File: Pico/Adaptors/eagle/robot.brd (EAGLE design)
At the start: 63.9 x 22.1 mm, 23 parts, among them J1 JST-2P-SMD-PW-3410050P1, U1 HC_05

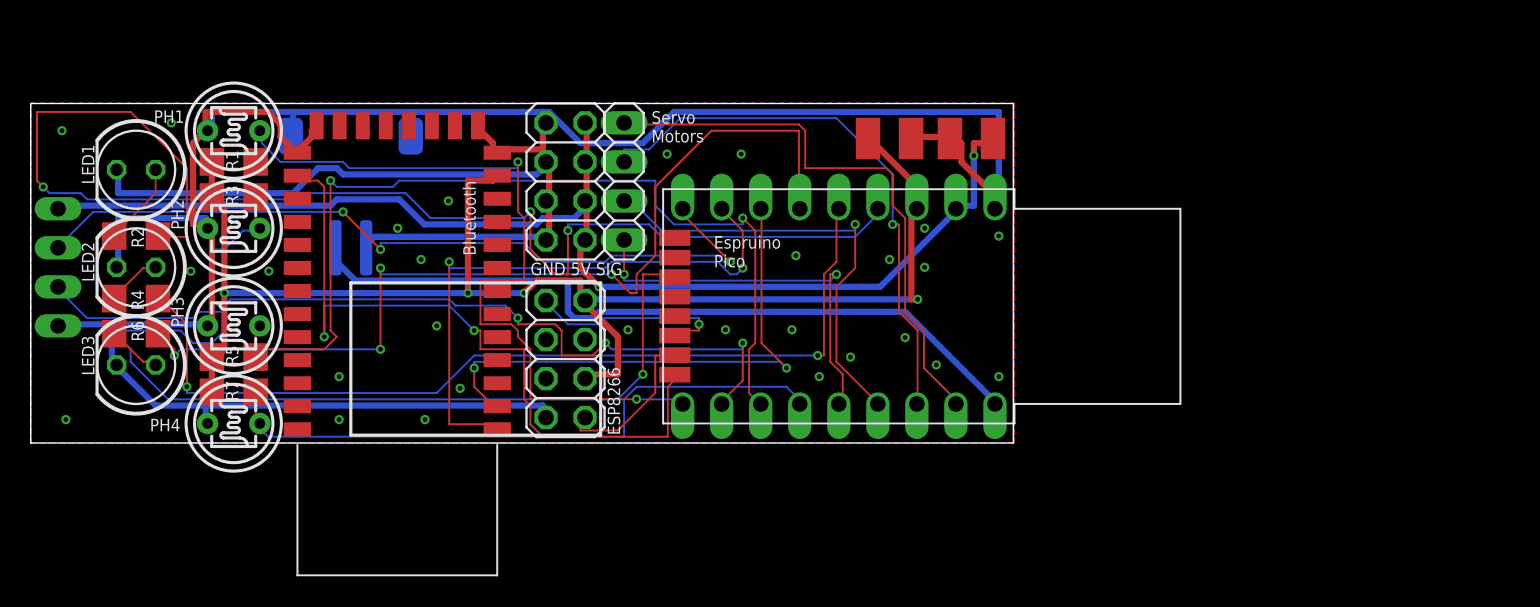
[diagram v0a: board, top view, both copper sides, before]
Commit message: added another ultrasonic sensor, pins down the side, and ADNS5050 optical sensor
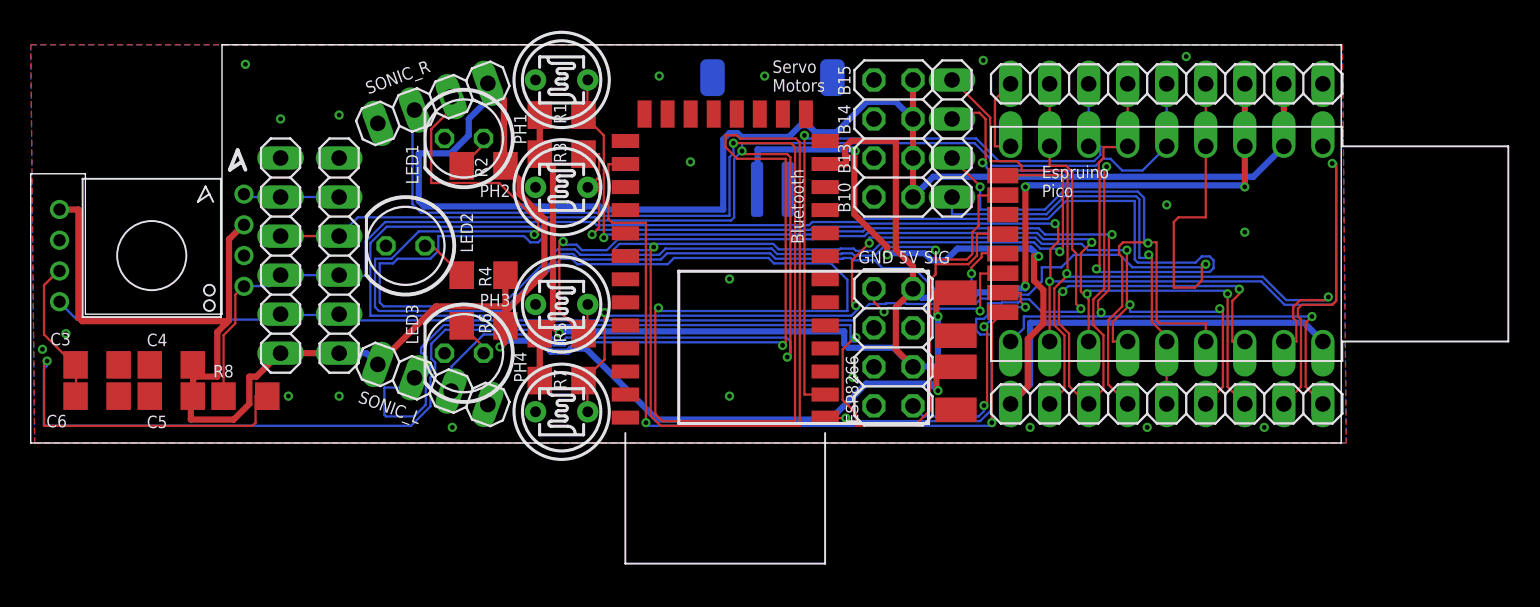
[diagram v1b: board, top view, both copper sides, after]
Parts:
- removed HC-SR04: (no value), pinhead:1X04
- added C3: 3.3uF, rcl:C1206
- added C4: 4.7uF, rcl:C1206
- added C5, C6: 0.1uF, rcl:C1206
- added JP3, JP4: (no value), pinhead:1X06
- added JP5, JP6: (no value), pinhead:1X09
- added R8: 3k, rcl:R1206
- added SONIC_L, SONIC_R: (no value), pinhead:1X04
- added U$2: ADNS5050, adns5050:ADNS-5050
- moved J1 27.7 mm to (48.3, 21.6)
- moved R2 23.1 mm to (29.5, 18.0)
- moved R4 22.7 mm to (29.5, 10.9)
- moved R6 22.6 mm to (29.5, 7.62)
- moved U$1 21.7 mm to (71.4, 13.0)
- moved PH1 21.6 mm to (34.5, 23.6)
- moved R1 21.6 mm to (34.5, 21.3)
- moved JP2 21.5 mm to (59.9, 19.8)
- moved JP1 21.5 mm to (56.1, 19.8)
- moved R3 21.5 mm to (34.5, 18.8)
- moved PH2 21.5 mm to (34.5, 16.6)
- moved LED1 21.4 mm to (28.2, 19.8)
- moved R5 21.4 mm to (34.5, 7.11)
- moved PH3 21.4 mm to (34.5, 9.02)
- moved ESP8266 21.3 mm to (56.1, 6.22)
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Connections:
- removed net HCSR04_ECHO: HC-SR04.3, U$1.A10
- removed net HCSR04_TRIG: HC-SR04.2, U$1.A8
- removed net LED1: R2.2, U$1.B3
- removed net LED2: R4.2, U$1.B4
- removed net LED3: R6.2, U$1.B5
- new net ADNS_MISO: JP3.4, JP4.4, JP6.5, R8.1, U$1.B4
- new net ADNS_MOSI: JP3.3, JP4.3, JP6.4, R8.2, U$1.B5, U$2.P$1
- new net ADNS_NCS: JP3.5, JP4.5, U$2.P$4
- new net ADNS_SCLK: JP3.2, JP4.2, JP6.6, U$1.B3, U$2.P$8
- new net N$1: JP6.1, U$1.A8
- new net N$2: C3.1, C6.1, U$2.P$7
- new net SONIC_L_ECHO: SONIC_L.3, U$1.B8
- new net SONIC_L_TRIG: SONIC_L.2, U$1.A0
- new net SONIC_R_ECHO: SONIC_R.3, U$1.B9
- new net SONIC_R_TRIG: SONIC_R.2, U$1.A1
- net 3.3V: now also JP6.7
- net 5V: now also C4.1, C5.1, JP3.1, JP4.1, JP6.8, R2.2, R4.2, R6.2, SONIC_L.1, SONIC_R.1, U$2.P$3, U$2.P$5; no longer HC-SR04.1
- net BT_RX: now also JP6.3
- net BT_TX: now also JP6.2
- net GND: now also C3.2, C4.2, C5.2, C6.2, JP3.6, JP4.6, JP6.9, SONIC_L.4, SONIC_R.4, U$2.P$6; no longer HC-SR04.4
- net LDR1: now also JP5.9
- net LDR2: now also JP5.8
- net LDR3: now also JP5.7
- net LDR4: now also JP5.6
- net SERVO1: now also JP5.5
- net SERVO2: now also JP5.4
- net SERVO3: now also JP5.3
- net SERVO4: now also JP5.2
- net VIN: now also JP5.1
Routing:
- net GND: track 210.1 -> 0.00 mm, vias 28 -> 21
- net SONIC_R_ECHO: track 0.00 -> 197.5 mm, vias 0 -> 3
- net ADNS_MISO: track 0.00 -> 165.9 mm, vias 0 -> 3
- net SONIC_L_ECHO: track 0.00 -> 128.1 mm, vias 0 -> 3
- net 5V: track 79.9 -> 203.8 mm
- net ADNS_MOSI: track 0.00 -> 101.1 mm, vias 0 -> 1
- net ADNS_SCLK: track 0.00 -> 96.7 mm, vias 0 -> 1
- net LED1: track 86.1 -> 0.00 mm, vias 3 -> 0
- net SONIC_R_TRIG: track 0.00 -> 75.5 mm, vias 0 -> 2
- net SONIC_L_TRIG: track 0.00 -> 69.0 mm, vias 0 -> 1
- net HCSR04_ECHO: track 67.0 -> 0.00 mm, vias 1 -> 0
- net LED3: track 61.7 -> 0.00 mm, vias 4 -> 0
- net LED2: track 59.4 -> 0.00 mm, vias 2 -> 0
- net HCSR04_TRIG: track 51.7 -> 0.00 mm, vias 3 -> 0
- net LDR2: track 52.1 -> 93.2 mm, vias 3 -> 4
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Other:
- board size 63.9 x 22.1 mm -> 85.3 x 25.9 mm
- board text added: "B10"
- board text added: "B13"
- board text added: "B14"
- board text added: "B15"

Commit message: misc tweaks
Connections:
- net ADNS_NCS: now also U$1.A10
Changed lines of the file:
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@@
 <wire x1="13.9192" y1="16.1544" x2="13.874" y2="16.192" width="0.1524" layer="16"/>
 <wire x1="16.256" y1="16.002" x2="20.066" y2="16.002" width="0.1524" layer="16"/>
+<contactref element="U$1" pad="A10"/>
+<wire x1="20.066" y1="16.002" x2="63.246" y2="14.859" width="0" layer="19" extent="1-1"/>
 </signal>
 <signal name="SONIC_R_ECHO">
